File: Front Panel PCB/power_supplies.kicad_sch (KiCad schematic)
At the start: 47 parts, among them J2 Main Power In, U10 LM317_TO-220, U11 LM337_TO220, U7 LMR36520FADDAR, U8 LMR36520FADDAR, U9 TLV75533PDBVR

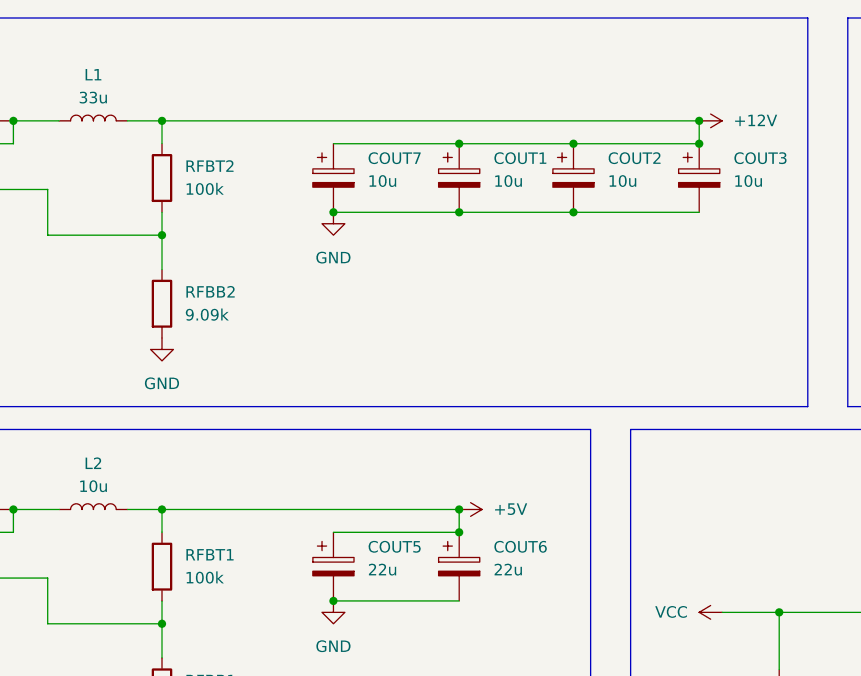
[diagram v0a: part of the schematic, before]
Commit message: Output Stage Schematic Created and complete. Next: Integrate STM32
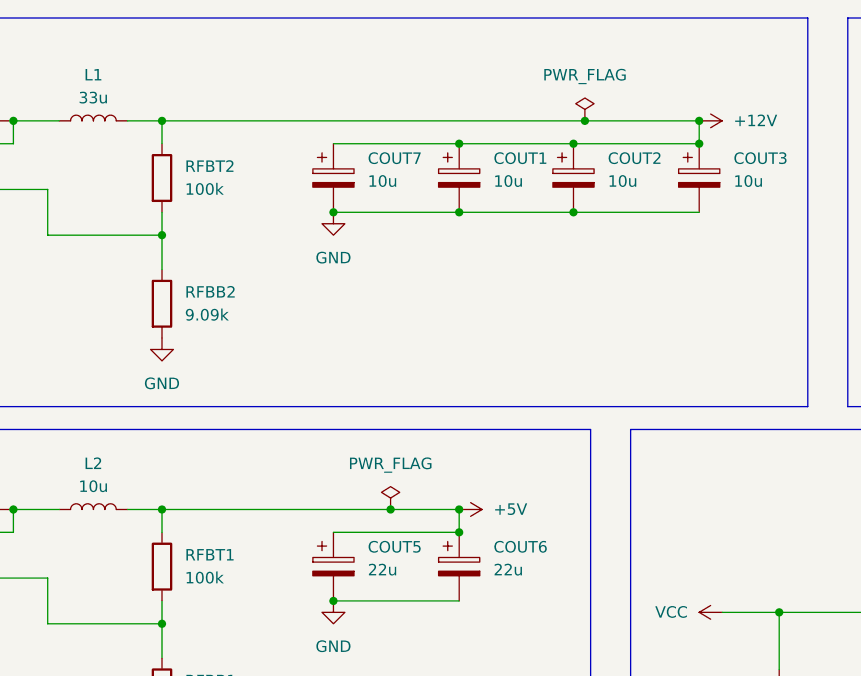
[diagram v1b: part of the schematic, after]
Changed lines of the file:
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@@
 	)
 	(junction
+		(at 172.72 27.94)
+		(diameter 0)
+		(color 0 0 0 0)
+	)
+	(junction
 		(at 55.88 27.94)
 		(diameter 0)
@@
 	)
 	(junction
+		(at 151.13 71.12)
+		(diameter 0)
+		(color 0 0 0 0)
+	)
+	(junction
 		(at 34.29 165.1)
 		(diameter 0)
@@
 	(wire
 		(pts
-			(xy 125.73 27.94) (xy 185.42 27.94)
+			(xy 125.73 27.94) (xy 172.72 27.94)
 		)
 		(stroke
@@
 	(wire
 		(pts
+			(xy 151.13 71.12) (xy 158.75 71.12)
+		)
+		(stroke
+			(width 0)
+			(type default)
+		)
+	)
+	(wire
+		(pts
 			(xy 250.19 38.1) (xy 250.19 39.37)
 		)
@@
 	(wire
 		(pts
+			(xy 172.72 27.94) (xy 185.42 27.94)
+		)
+		(stroke
+			(width 0)
+			(type default)
+		)
+	)
+	(wire
+		(pts
 			(xy 72.39 162.56) (xy 72.39 165.1)
 		)
@@
 	(wire
 		(pts
-			(xy 125.73 71.12) (xy 158.75 71.12)
+			(xy 125.73 71.12) (xy 151.13 71.12)
 		)
 		(stroke
@@
 	)
 	(symbol
+		(lib_id "power:PWR_FLAG")
+		(at 151.13 71.12 0)
+		(unit 1)
+		(body_style 1)
+		(exclude_from_sim no)
+		(in_bom yes)
+		(on_board yes)
+		(in_pos_files yes)
+		(dnp no)
+		(fields_autoplaced yes)
+		(property "Reference" "#FLG05"
+			(at 151.13 69.215 0)
+			(hide yes)
+			(show_name no)
+			(do_not_autoplace no)
+			(effects
+				(font
+					(size 1.27 1.27)
+				)
+			)
+		)
+		(property "Value" "PWR_FLAG"
+			(at 151.13 66.04 0)
+			(show_name no)
+			(do_not_autoplace no)
+			(effects
+				(font
+					(size 1.27 1.27)
+				)
+			)
+		)
+		(property "Footprint" ""
+			(at 151.13 71.12 0)
+			(hide yes)
+			(show_name no)
+			(do_not_autoplace no)
+			(effects
+				(font
+					(size 1.27 1.27)
+				)
+			)
+		)
+		(property "Datasheet" ""
+			(at 151.13 71.12 0)
+			(hide yes)
+			(show_name no)
+			(do_not_autoplace no)
+			(effects
+				(font
+					(size 1.27 1.27)
+				)
+			)
+		)
+		(property "Description" "Special symbol for telling ERC where power comes from"
+			(at 151.13 71.12 0)
+			(hide yes)
+			(show_name no)
+			(do_not_autoplace no)
+			(effects
+				(font
+					(size 1.27 1.27)
+				)
+			)
+		)
+		(pin "1"
+		)
+		(instances
+			(project "FrontPanelDesign"
+				(path "/79626054-a4b7-4da2-97a1-0bdbb09a0a07"
+					(reference "#FLG05")
+					(unit 1)
+				)
+			)
+		)
+	)
+	(symbol
 		(lib_id "Diode:1N4007")
 		(at 231.14 90.17 270)
@@
 					(unit 1)
 				)
+			)
+		)
+	)
+	(symbol
+		(lib_id "power:PWR_FLAG")
+		(at 172.72 27.94 0)
+		(unit 1)
+		(body_style 1)
+		(exclude_from_sim no)
+		(in_bom yes)
+		(on_board yes)
+		(in_pos_files yes)
+		(dnp no)
+		(fields_autoplaced yes)
+		(property "Reference" "#FLG04"
+			(at 172.72 26.035 0)
+			(hide yes)
+			(show_name no)
+			(do_not_autoplace no)
+			(effects
+				(font
+					(size 1.27 1.27)
+				)
+			)
+		)
+		(property "Value" "PWR_FLAG"
+			(at 172.72 22.86 0)
+			(show_name no)
+			(do_not_autoplace no)
+			(effects
+				(font
+					(size 1.27 1.27)
+				)
+			)
+		)
+		(property "Footprint" ""
+			(at 172.72 27.94 0)
+			(hide yes)
+			(show_name no)
+			(do_not_autoplace no)
+			(effects
+				(font
+					(size 1.27 1.27)
+				)
+			)
+		)
+		(property "Datasheet" ""
+			(at 172.72 27.94 0)
+			(hide yes)
+			(show_name no)
+			(do_not_autoplace no)
+			(effects
+				(font
+					(size 1.27 1.27)
+				)
+			)
+		)
+		(property "Description" "Special symbol for telling ERC where power comes from"
+			(at 172.72 27.94 0)
+			(hide yes)
+			(show_name no)
+			(do_not_autoplace no)
+			(effects
+				(font
+					(size 1.27 1.27)
+				)
+			)
+		)
+		(pin "1"
+		)
+		(instances
+			(project "FrontPanelDesign"
+				(path "/79626054-a4b7-4da2-97a1-0bdbb09a0a07"
+					(reference "#FLG04")
+					(unit 1)
+				)

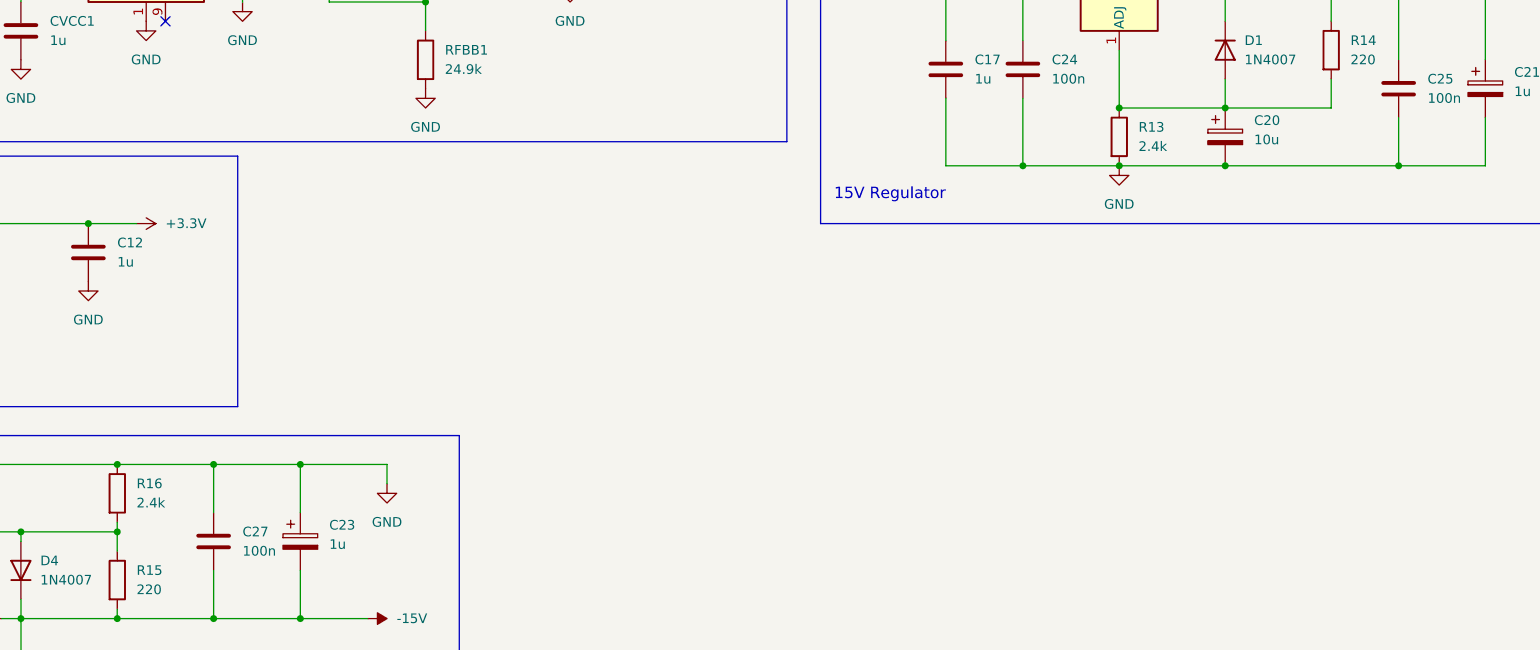
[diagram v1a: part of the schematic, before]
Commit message: Bill of materials ETC finalised, selecting footprints next
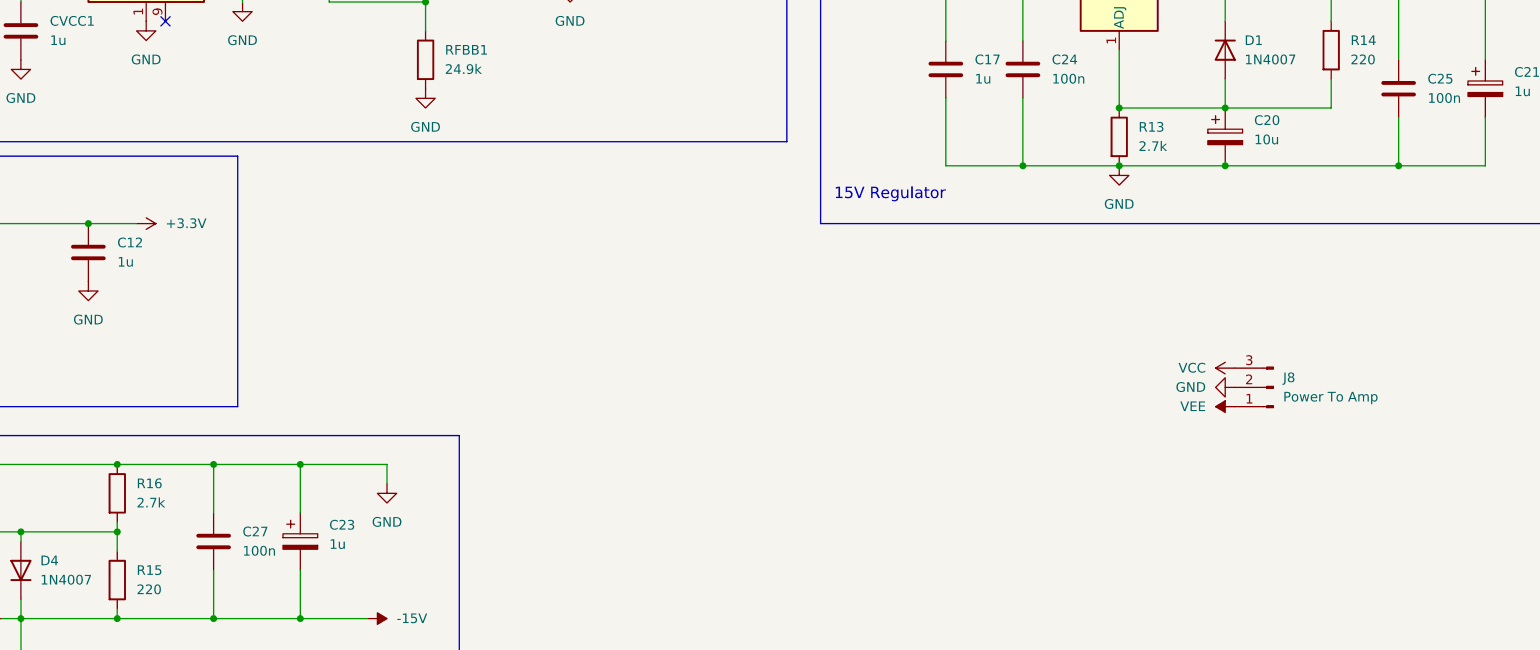
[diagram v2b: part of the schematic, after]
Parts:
- added J8: Power To Amp, symbol Connector:Conn_01x03_Pin
- R13, R16: value 2.4k -> 2.7k
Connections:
- net GND: now also J8.2 (Pin_2)
- net VCC: now also J8.3 (Pin_3)
- net VEE: now also J8.1 (Pin_1)
